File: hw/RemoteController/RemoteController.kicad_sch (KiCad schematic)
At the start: 67 parts, among them J1 Conn_01x04_Pin, J2 Conn_01x04_Pin, SW2 ST-0-102-A01-T000-LF, SW6 TS-1088-AR02016, SW7 TS-1088-AR02016, SW8 TS-1088-AR02016, SW9 TS-1088-AR02016, U1 LM358, U11 LM358, U13 nRF52810-QFxx, U14 LM358, U15 LM358, U2 TPS562200, Y1 32 MHz, Y5 32.768 KHz

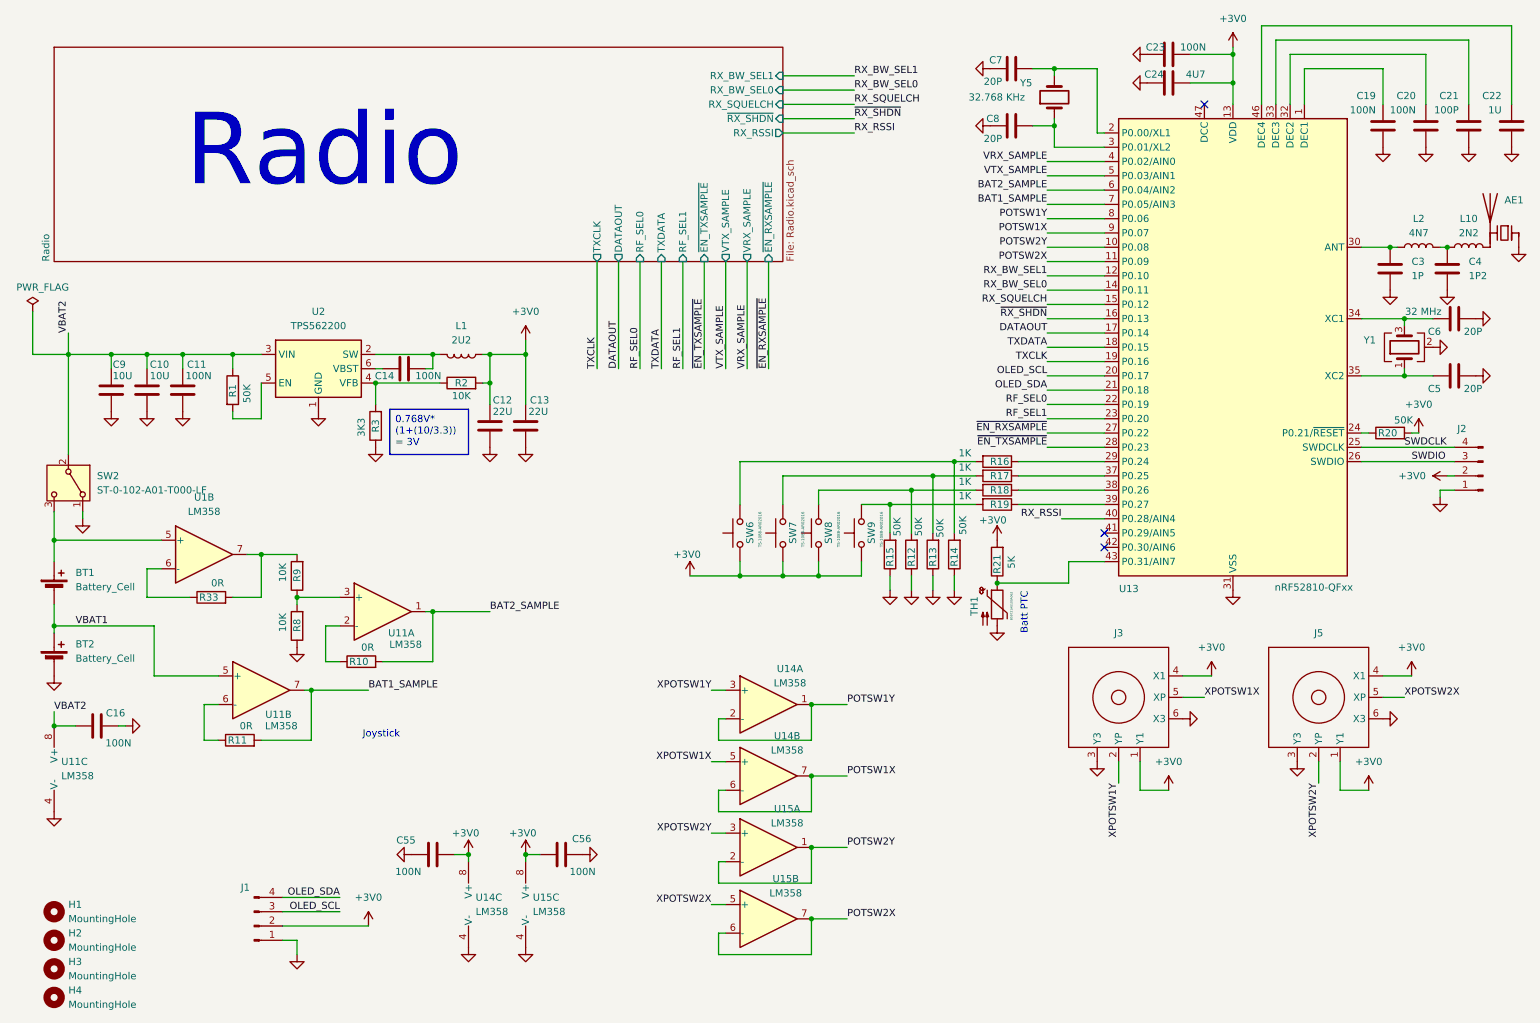
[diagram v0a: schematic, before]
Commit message: remote_ctrl: change logdet to AD8314 and battery holder to SMD
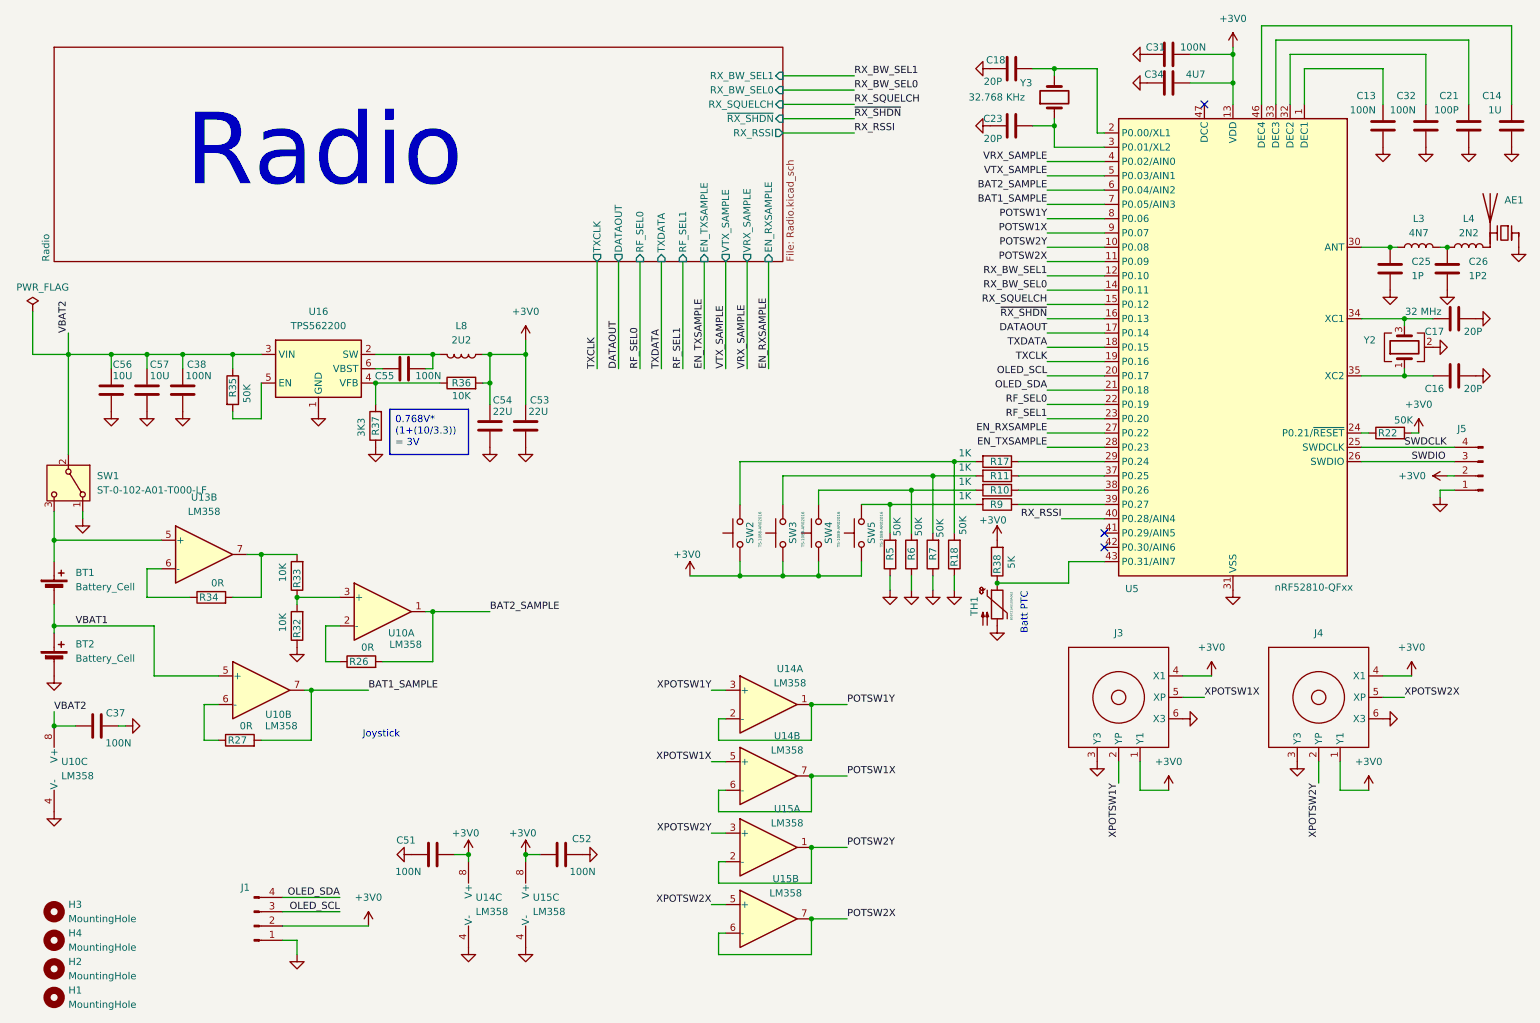
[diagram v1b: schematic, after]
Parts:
- AE1, TH1: KiLib_Generator (none) -> SMD_2terminal_chip_molded
- BT1, BT2: footprint Battery:BatteryHolder_Bulgin_BX0034_1xAAA -> steew:BH-AAA-B5BA021
- C16: renamed from C5; KiLib_Generator (none) -> SMD_2terminal_chip_molded
- C17: renamed from C6; KiLib_Generator (none) -> SMD_2terminal_chip_molded
- C18: renamed from C7; KiLib_Generator (none) -> SMD_2terminal_chip_molded
- C23: renamed from C8; KiLib_Generator (none) -> SMD_2terminal_chip_molded
- C25: renamed from C3; KiLib_Generator (none) -> SMD_2terminal_chip_molded
- C26: renamed from C4; KiLib_Generator (none) -> SMD_2terminal_chip_molded
- H1: renamed from H4; KiLib_Generator (none) -> mounting_hardware/mounting_hole
- H2: renamed from H3; KiLib_Generator (none) -> mounting_hardware/mounting_hole
- H3: renamed from H1; KiLib_Generator (none) -> mounting_hardware/mounting_hole
- H4: renamed from H2; KiLib_Generator (none) -> mounting_hardware/mounting_hole
- J1: KiLib_Generator (none) -> connector/pin_header_socket
- J5: renamed from J2; KiLib_Generator (none) -> connector/JST
- L3: renamed from L2; KiLib_Generator (none) -> SMD_2terminal_chip_molded
- L4: renamed from L10; KiLib_Generator (none) -> SMD_2terminal_chip_molded
- U13: renamed from U1; KiLib_Generator (none) -> package/gullwing
- U14, U15: KiLib_Generator (none) -> package/gullwing
- U5: renamed from U13; KiLib_Generator (none) -> package/no_lead
- Y2: renamed from Y1; KiLib_Generator (none) -> crystal_resonator_oscillator; private KLC_S3.3 -> (none)
- renumbered C19 to C13, C22 to C14, C23 to C31, C20 to C32, C24 to C34, C16 to C37, C11 to C38, C55 to C51, C56 to C52, C13 to C53, C12 to C54, C14 to C55, C9 to C56, C10 to C57, J5 to J4, L1 to L8, R18 to R10, R17 to R11, R16 to R17, R14 to R18, R20 to R22, R10 to R26, R11 to R27, R8 to R32, R9 to R33, R33 to R34, R1 to R35, R2 to R36, R3 to R37, R21 to R38, R15 to R5, R12 to R6, R13 to R7, R19 to R9, SW2 to SW1, SW6 to SW2, SW7 to SW3, SW8 to SW4, SW9 to SW5, U11 to U10, U2 to U16, Y5 to Y3
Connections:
- net ~{EN_RXSAMPLE} renamed EN_RXSAMPLE
- net ~{EN_TXSAMPLE} renamed EN_TXSAMPLE
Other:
- sheet Radio ports: added EN_RXSAMPLE, EN_TXSAMPLE; removed ~{EN_RXSAMPLE}, ~{EN_TXSAMPLE}
